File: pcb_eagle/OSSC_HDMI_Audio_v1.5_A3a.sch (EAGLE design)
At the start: 29 parts, among them U1 PCM1808, U2 74LVC1G34, U3 MK2507SLF

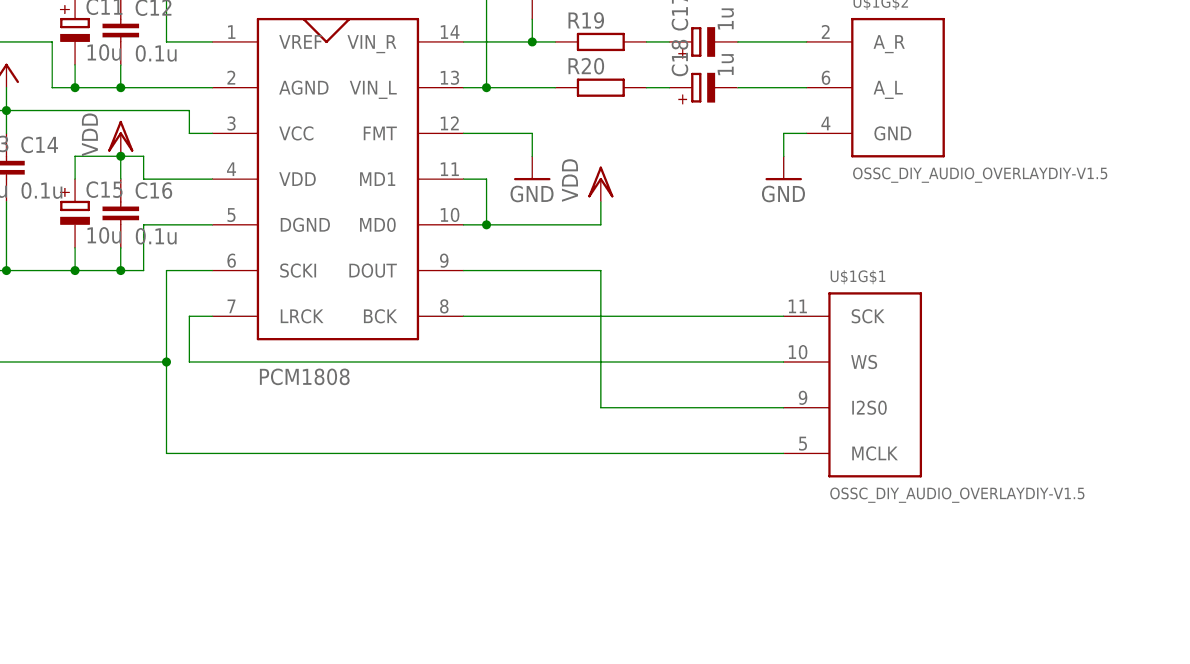
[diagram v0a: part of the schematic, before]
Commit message: External Masterclock option removed in OSSC firmware v0.75 - PCB files back to A3 - backed up A4 in additional sub-folder
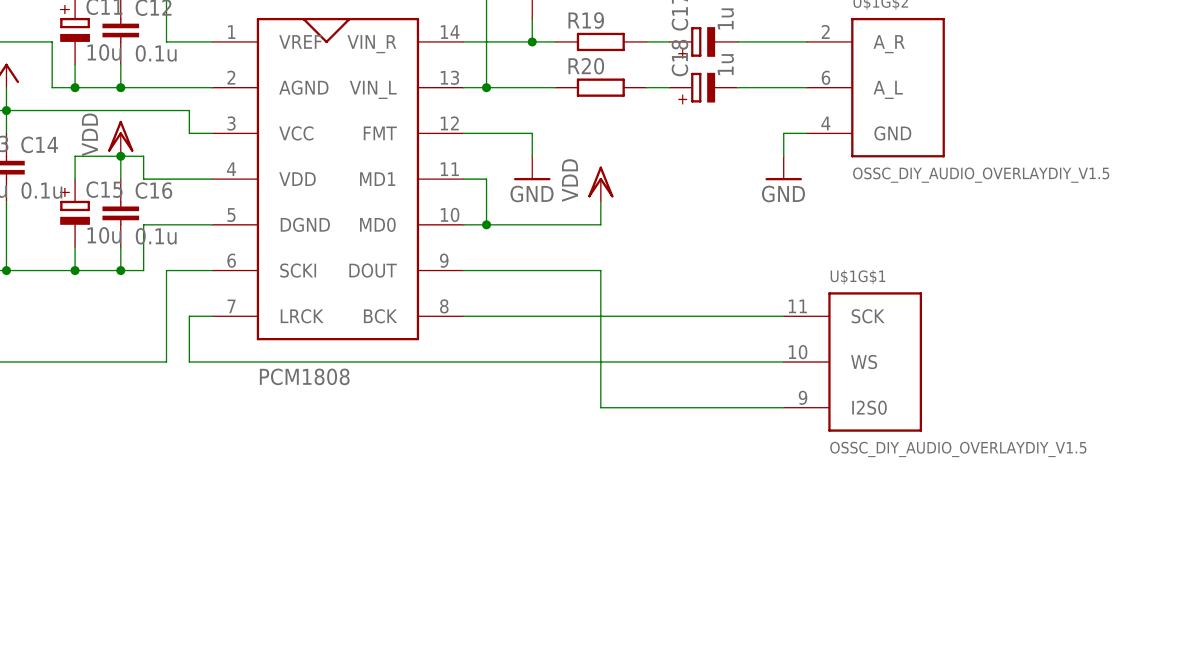
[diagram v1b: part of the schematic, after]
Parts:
- U$1: value OSSC_DIY_AUDIO_OVERLAYDIY-V1.5 -> OSSC_DIY_AUDIO_OVERLAYDIY_V1.5; device OSSC_HDMI_Audio:OSSC_DIY_AUDIO_OVERLAYDIY-V1.5 -> OSSC_HDMI_Audio:OSSC_DIY_AUDIO_OVERLAYDIY_V1.5
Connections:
- net N$17: no longer U$1G$1.MCLK
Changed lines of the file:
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@@
 <?xml version="1.0" encoding="utf-8"?>
 <!DOCTYPE eagle SYSTEM "eagle.dtd">
-<eagle version="7.6.0">
+<eagle version="7.7.0">
 <drawing>
 <settings>
@@
 <part name="FB2" library="rcl" deviceset="R-EU_" device="R0603"/>
 <part name="U2" library="OSSC_HDMI_Audio" deviceset="74LVC1G34" device=""/>
-<part name="U$1" library="OSSC_HDMI_Audio" deviceset="OSSC_DIY_AUDIO_OVERLAY" device="DIY-V1.5" value="OSSC_DIY_AUDIO_OVERLAYDIY-V1.5"/>
+<part name="U$1" library="OSSC_HDMI_Audio" deviceset="OSSC_DIY_AUDIO_OVERLAY" device="DIY_V1.5"/>
 </parts>
 <sheets>
@@
 <instance part="U2" gate="G$1" x="22.86" y="30.48"/>
 <instance part="U2" gate="G$2" x="83.82" y="48.26"/>
+<instance part="U$1" gate="G$2" x="208.28" y="60.96"/>
 <instance part="U$1" gate="G$1" x="205.74" y="27.94"/>
-<instance part="U$1" gate="G$2" x="208.28" y="60.96"/>
 </instances>
 <busses>
@@
 <pinref part="GND1" gate="1" pin="GND"/>
 <wire x1="198.12" y1="55.88" x2="198.12" y2="53.34" width="0.1524" layer="91"/>
+<wire x1="198.12" y1="55.88" x2="200.66" y2="55.88" width="0.1524" layer="91"/>
 <pinref part="U$1" gate="G$2" pin="GND"/>
-<wire x1="198.12" y1="55.88" x2="200.66" y2="55.88" width="0.1524" layer="91"/>
 </segment>
 <segment>
@@
 <segment>
 <pinref part="C18" gate="G$1" pin="-"/>
+<wire x1="200.66" y1="60.96" x2="193.04" y2="60.96" width="0.1524" layer="91"/>
 <pinref part="U$1" gate="G$2" pin="A_L"/>
-<wire x1="200.66" y1="60.96" x2="193.04" y2="60.96" width="0.1524" layer="91"/>
 </segment>
 </net>
@@
 <segment>
 <pinref part="C17" gate="G$1" pin="-"/>
+<wire x1="200.66" y1="66.04" x2="193.04" y2="66.04" width="0.1524" layer="91"/>
 <pinref part="U$1" gate="G$2" pin="A_R"/>
-<wire x1="200.66" y1="66.04" x2="193.04" y2="66.04" width="0.1524" layer="91"/>
 </segment>
 </net>
@@
 <pinref part="R31" gate="G$1" pin="2"/>
 <wire x1="129.54" y1="30.48" x2="91.44" y2="30.48" width="0.1524" layer="91"/>
-<pinref part="U$1" gate="G$1" pin="MCLK"/>
-<wire x1="198.12" y1="20.32" x2="129.54" y2="20.32" width="0.1524" layer="91"/>
-<wire x1="129.54" y1="20.32" x2="129.54" y2="30.48" width="0.1524" layer="91"/>
-<junction x="129.54" y="30.48"/>
-</segment>
-</net>
+</segment>
+</net>
